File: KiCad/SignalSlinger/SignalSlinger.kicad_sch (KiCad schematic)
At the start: 65 parts, among them J101 Conn_01x02, J103 Conn_01x02, J104 Conn_01x02, J105 Conn_01x02, J106 Conn_01x02, J107 DB9 Female, J108 Conn_01x02, J109 Conn_01x03, J110 Conn_01x02, J111 Conn_01x03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

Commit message: Updates
o Updated Gerbers
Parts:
- removed C116: 10uF, Capacitor_SMD:C_0805_2012Metric, symbol Device:C_Small
- removed J105: Conn_01x02, Connector_PinSocket_2.54mm:PinSocket_1x02_P2.54mm_Vertical, symbol Connector_Generic:Conn_01x02
- removed J112: External Power Source, Connector_PinHeader_2.54mm:PinHeader_1x02_P2.54mm_Vertical, symbol Connector_Generic:Conn_01x02
- removed J113: Controlled Power, Connector_PinHeader_2.54mm:PinHeader_1x02_P2.54mm_Vertical, symbol Connector_Generic:Conn_01x02
- removed JP101: V-ext disable, Jumper:SolderJumper-2_P1.3mm_Bridged_RoundedPad1.0x1.5mm, symbol Jumper:SolderJumper_2_Bridged
- removed U105: TPS22810DBVT, Package_TO_SOT_SMD:SOT-23-6, symbol Power_Management:TPS22810DBVT
- added D111, D112: ESD9B5.0ST5G_1, Diode_SMD:D_0603_1608Metric, symbol Diode:ESD9B5.0ST5G_1
- added J102: Conn_01x03, Connector_PinHeader_2.54mm:PinHeader_1x03_P2.54mm_Vertical, symbol Connector_Generic:Conn_01x03
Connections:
- net GND: now also D111.2 (A2), D112.2 (A2), J102.2 (Pin_2)
- net Power_Good: now also U101.7 (PD1); no longer U101.11 (PD5)
- net Frequency Up: now reaches U101.12 (PD6/DAC)
- net Frequency Up: now also J107.4, D111.1 (A1), J102.3 (Pin_3)
- net Frequency Down: now reaches U101.13 (PD7)
- net Frequency Down: now also J107.5, D112.1 (A1), J102.1 (Pin_1)
- no-connect marks 18 -> 13
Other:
- note removed: "OPTIONAL AUX CONTROL"
- moved on the sheet: C104, D101, D102, D103, D104, D105, D106, D108, D109, D110, J101, J103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

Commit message: KiCad Updates
Updated Gerbers and schematic
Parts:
- added J105: Conn_01x04, Connector_PinHeader_2.54mm:PinHeader_1x04_P2.54mm_Vertical, symbol Connector_Generic:Conn_01x04
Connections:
- net GND: now also J105.1 (Pin_1)
- net Paddle Dah: now also J105.3 (Pin_3)
- net Paddle_Dit: now also J105.2 (Pin_2)
- net Straightkey: now also J105.4 (Pin_4)
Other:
- note added: "L101: 9T (24 cm) #24 Bifilar FT-50A-43"
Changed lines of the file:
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@@
     (effects (font (size 1.27 1.27)) (justify left bottom))
   )
+  (text "L101:\n9T (24 cm) #24 Bifilar FT-50A-43" (at 256.54 68.58 0)
+    (effects (font (size 0.9906 0.9906) (thickness 0.1981) bold) (justify left bottom))
+  )
   (text "I2C pull-ups can be provided by uC \nport pin pull-ups on SCL and SDA."
     (at 154.94 88.9 0)
@@
     )
   )
+  (global_label "Straightkey" (shape input) (at 160.02 175.26 0) (fields_autoplaced)
+    (effects (font (size 1 1)) (justify left))
+    (property "Intersheet References" "${INTERSHEET_REFS}" (id 0) (at 170.2533 175.1975 0)
+      (effects (font (size 1 1)) (justify left) hide)
+    )
+  )
   (global_label "CLK1" (shape output) (at 175.26 60.96 0) (fields_autoplaced)
     (effects (font (size 0.9906 0.9906)) (justify left))
@@
     )
   )
+  (global_label "Paddle_Dit" (shape input) (at 160.02 170.18 0) (fields_autoplaced)
+    (effects (font (size 1 1)) (justify left))
+    (property "Intersheet References" "${INTERSHEET_REFS}" (id 0) (at 169.8248 170.1175 0)
+      (effects (font (size 1 1)) (justify left) hide)
+    )
+  )
   (global_label "FET_DRIVER_ENABLE" (shape output) (at 80.01 71.12 0) (fields_autoplaced)
     (effects (font (size 0.9906 0.9906)) (justify left))
@@
     )
   )
+  (global_label "Paddle Dah" (shape input) (at 160.02 172.72 0) (fields_autoplaced)
+    (effects (font (size 1 1)) (justify left))
+    (property "Intersheet References" "${INTERSHEET_REFS}" (id 0) (at 170.5867 172.6575 0)
+      (effects (font (size 1 1)) (justify left) hide)
+    )
+  )
   (global_label "Fan_Contr" (shape output) (at 44.45 111.76 180) (fields_autoplaced)
     (effects (font (size 0.9906 0.9906)) (justify right))
@@
     (pin "1")
   )
+  (symbol (lib_id "power:GND") (at 160.02 167.64 90) (unit 1)
+    (in_bom yes) (on_board yes) (fields_autoplaced)
+    (property "Reference" "#PWR0166" (id 0) (at 166.37 167.64 0)
+      (effects (font (size 1.27 1.27)) hide)
+    )
+    (property "Value" "GND" (id 1) (at 164.4634 167.64 0)
+      (effects (font (size 1.27 1.27)) hide)
+    )
+    (property "Footprint" "" (id 2) (at 160.02 167.64 0)
+      (effects (font (size 1.27 1.27)) hide)
+    )
+    (property "Datasheet" "" (id 3) (at 160.02 167.64 0)
+      (effects (font (size 1.27 1.27)) hide)
+    )
+    (pin "1")
+  )
   (symbol (lib_id "Diode:ESD9B5.0ST5G_1") (at 139.7 137.16 270) (unit 1)
     (in_bom yes) (on_board yes) (fields_autoplaced)
@@
     (pin "2")
   )
+  (symbol (lib_id "Connector_Generic:Conn_01x04") (at 154.94 170.18 0) (mirror y) (unit 1)
+    (in_bom yes) (on_board yes) (fields_autoplaced)
+    (property "Reference" "J105" (id 0) (at 154.94 165.2072 0))
+    (property "Value" "Conn_01x04" (id 1) (at 154.94 165.2071 0)
+      (effects (font (size 1.27 1.27)) hide)
+    )
+    (property "Footprint" "Connector_PinHeader_2.54mm:PinHeader_1x04_P2.54mm_Vertical" (id 2) (at 154.94 170.18 0)
+      (effects (font (size 1.27 1.27)) hide)
+    )
+    (property "Datasheet" "~" (id 3) (at 154.94 170.18 0)
+      (effects (font (size 1.27 1.27)) hide)
+    )
+    (pin "1")
+    (pin "2")
+    (pin "3")
+    (pin "4")
+  )
   (symbol (lib_id "Device:C_Small") (at 260.35 57.15 90) (unit 1)
     (in_bom yes) (on_board yes)
@@
       (reference "#PWR0164") (unit 1) (value "GND") (footprint "")
     )
+    (path "/b7c888bf-e50e-45b8-8886-9bc5abf637fe/f25afcc1-fcb9-4c17-a20d-0ea083f083ef"
+      (reference "#PWR0165") (unit 1) (value "+3V3") (footprint "")
+    )
+    (path "/550b26c9-1cee-47c6-81a9-45e6d70bb39c"
+      (reference "#PWR0166") (unit 1) (value "GND") (footprint "")
+    )
     (path "/b7c888bf-e50e-45b8-8886-9bc5abf637fe/80c237a1-ee53-4ac9-8ec4-43aca92dc707"
       (reference "#PWR0201") (unit 1) (value "GND") (footprint "")
@@
     )
     (path "/b7c888bf-e50e-45b8-8886-9bc5abf637fe/01d30a66-451a-43fd-95f2-0bdd2117103d"
-      (reference "C213") (unit 1) (value "22uF") (footprint "Capacitor_SMD:C_1210_3225Metric")
+      (reference "C213") (unit 1) (value "22uF") (footprint "Capacitor_SMD:C_0805_2012Metric")
     )
     (path "/b7c888bf-e50e-45b8-8886-9bc5abf637fe/ebba386f-ca53-469e-b170-4c68f88638d5"
-      (reference "C214") (unit 1) (value "22uF") (footprint "Capacitor_SMD:C_1210_3225Metric")
+      (reference "C214") (unit 1) (value "22uF") (footprint "Capacitor_SMD:C_0805_2012Metric")
     )
     (path "/b7c888bf-e50e-45b8-8886-9bc5abf637fe/5c012b10-83b8-496d-af4b-de5dc92abc05"
-      (reference "C215") (unit 1) (value "22uF") (footprint "Capacitor_SMD:C_1210_3225Metric")
+      (reference "C215") (unit 1) (value "22uF") (footprint "Capacitor_SMD:C_0805_2012Metric")
     )
     (path "/b7c888bf-e50e-45b8-8886-9bc5abf637fe/1e940795-b9b5-45f3-99c7-d1d40e53f1a6"
@@
       (reference "C301") (unit 1) (value "470nF") (footprint "Capacitor_SMD:C_0805_2012Metric")
     )
-    (path "/da189f43-fd1f-445a-980b-345fda8b9a74/1e903e0b-fffc-4a7b-9e11-b17f2dc58886"
+    (path "/da189f43-fd1f-445a-980b-345fda8b9a74/f0d89eae-86d0-4eee-82c6-ad3daf7543e5"
       (reference "C302") (unit 1) (value "1100pF") (footprint "Capacitor_THT:C_Rect_L7.0mm_W2.5mm_P5.00mm")
     )
@@
       (reference "J104") (unit 1) (value "Conn_01x02") (footprint "Connector_PinSocket_2.54mm:PinSocket_1x02_P2.54mm_Vertical")
     )
+    (path "/db76a492-e672-4dba-bea7-c36487286d56"
+      (reference "J105") (unit 1) (value "Conn_01x04") (footprint "Connector_PinHeader_2.54mm:PinHeader_1x04_P2.54mm_Vertical")
+    )
     (path "/aad2424a-3937-4bc7-96c8-78c666e64a3d"
       (reference "J106") (unit 1) (value "Conn_01x02") (footprint "Connector_PinSocket_2.54mm:PinSocket_1x02_P2.54mm_Vertical")
@@
     )
     (path "/b7c888bf-e50e-45b8-8886-9bc5abf637fe/b1a6cee7-c293-4248-bf6c-e4b6e388a068"
-      (reference "L201") (unit 1) (value "2.2uH") (footprint "Inductor_SMD:L_Wuerth_WE-LQS")
+      (reference "L201") (unit 1) (value "2.2uH") (footprint "Inductor_SMD:WPN4020H2R2MT")
     )
     (path "/b7c888bf-e50e-45b8-8886-9bc5abf637fe/0c5297a9-41d0-4223-b152-7bff564be51e"
@@
       (reference "R204") (unit 1) (value "1M") (footprint "Resistor_SMD:R_0805_2012Metric")
     )
-    (path "/b7c888bf-e50e-45b8-8886-9bc5abf637fe/a604157e-b596-422f-8a01-c3245280c807"
+    (path "/b7c888bf-e50e-45b8-8886-9bc5abf637fe/846f2c13-278f-48b2-82e1-5d1c7211b810"
       (reference "R205") (unit 1) (value "105k") (footprint "Resistor_SMD:R_0805_2012Metric")
     )

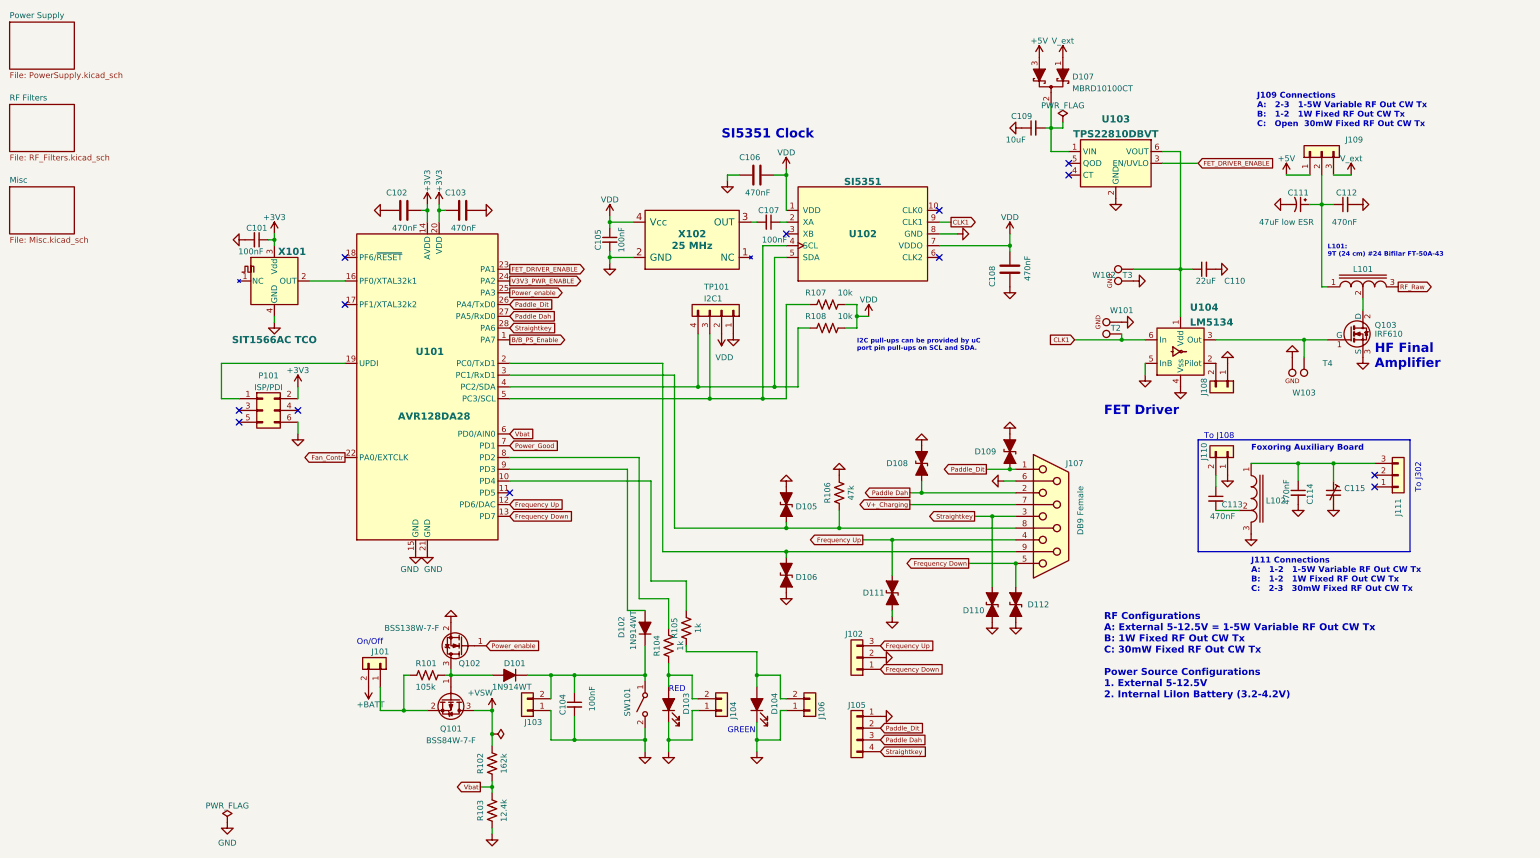
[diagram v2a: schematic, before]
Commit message: Schematic Updates
o Added support for a linear adjustable voltage regulator
o Added a switch
o Re-arranged components for a better fit
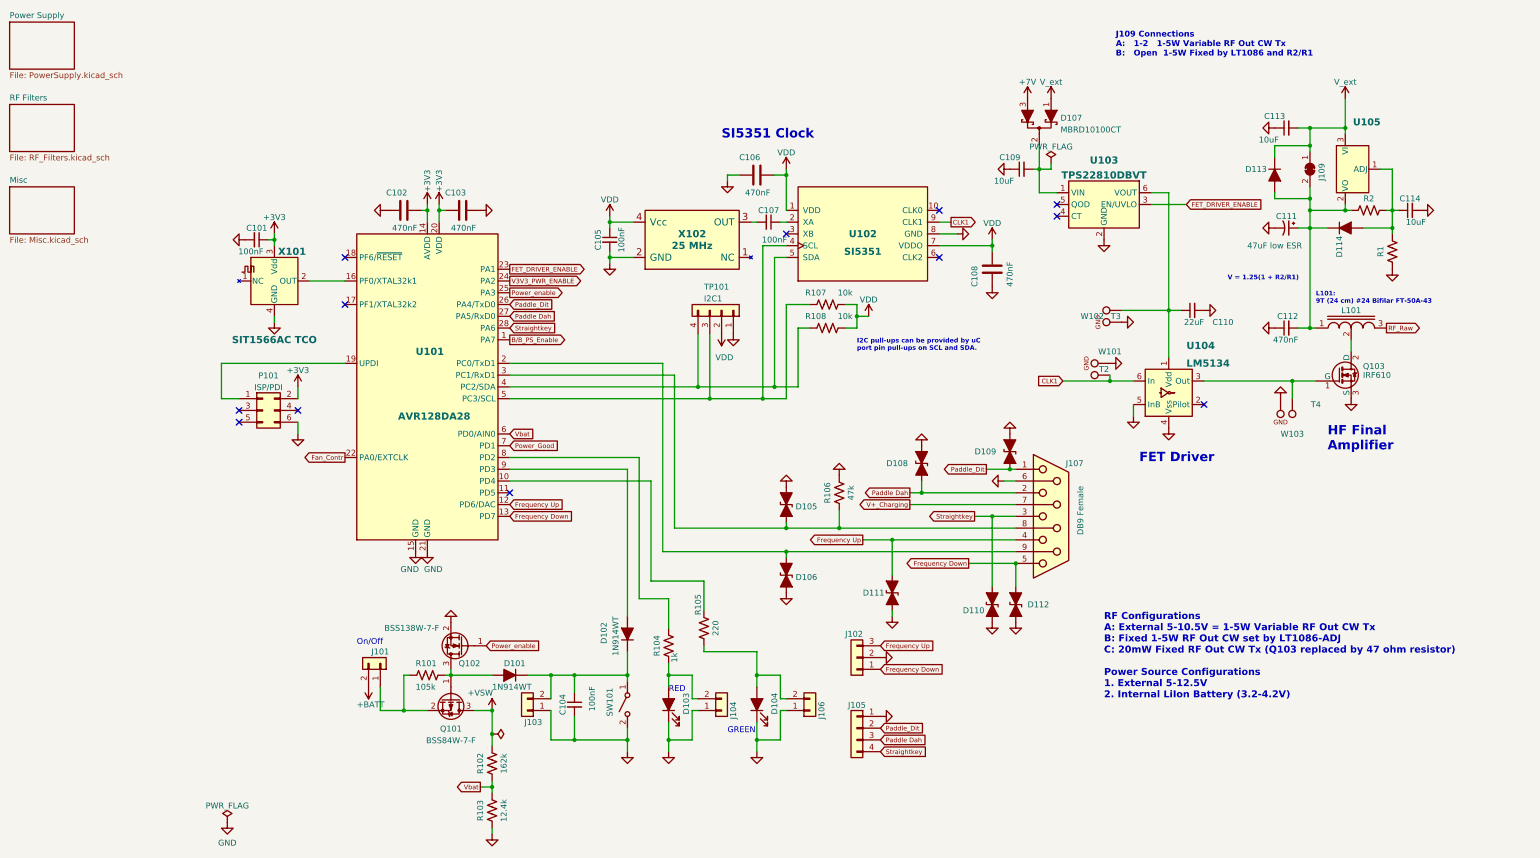
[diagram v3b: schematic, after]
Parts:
- removed C115: C_Trim_Small, Capacitors:MURATA-TZC3, symbol Device:C_Trim_Small
- removed J108, J110: Conn_01x02, Connector_PinHeader_2.54mm:PinHeader_1x02_P2.54mm_Vertical, symbol Connector_Generic:Conn_01x02
- removed J109, J111: Conn_01x03, Connector_PinHeader_2.54mm:PinHeader_1x03_P2.54mm_Vertical, symbol Connector_Generic:Conn_01x03
- removed L102: INDUCTOR_tapped, Inductors:Toroid_T-50A_TH_BF_CT_Vertical, symbol Device:INDUCTOR_tapped
- added D113, D114: 1N914WT, Diode_SMD:D_SOD-523, symbol Diode:1N914WT
- added J109: SolderJumper_2_Bridged, Jumper:SolderJumper-2_P1.3mm_Bridged_RoundedPad1.0x1.5mm, symbol Jumper:SolderJumper_2_Bridged
- added R1, R2: TBD, Resistor_THT:R_Axial_DIN0204_L3.6mm_D1.6mm_P2.54mm_Vertical, symbol Device:R_Small_US
- added U105: (no value), TO_SOT_Packages:TO-220_Neutral123_Horizontal, symbol Regulator_Linear:LT1086-ADJ
- C113, C114: value 470nF -> 10uF; Digi-Key Part No. 478-9924-1-ND -> 445-14418-1-ND; LCSC Part Number C342818 -> C3843628; Link https://www.digikey.com/products/en?keywords=478-9924-1-ND -> https://www.digikey.com/short/p8qdn4mp; Manufacturer AVX Corporation -> TDK Corporation; Manufacturer PN 08051C474K4Z2A -> C2012X5R1V106K125AC
- R105: value 1k -> 220; Digi-Key Part No. RMCF0805FT1K00CT-ND -> 13-RC0805FR-10220RLCT-ND; LCSC Part Number C17513 -> (none); Link https://www.digikey.com/en/products/detail/stackpole-electr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 -> https://www.digikey.com/en/products/detail/yageo/rc0805fr-1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; Manufacturer Stackpole Electronics Inc -> Yageo; Manufacturer PN RMCF0805FT1K00 -> RC0805FR-10220RL
- SW101: footprint Button_Switch_SMD:SW_SPST_B3U-3000P-B -> Button_Switch_SMD:SW_SPST_TL3305A; Digi-Key Part No. SW1256CT-ND -> EG5042CT-ND; Link (none) -> https://www.digikey.com/en/products/detail/e-switch/TL1014B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; Manufacturer Omron Electronics Inc-EMC Div -> E-Switch; Manufacturer PN B3U-3000P-B -> TL1014BF160QG
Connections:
- net GND: now also C112.1, C113.1, R1.1; no longer C112.2
- net V_ext: now also C113.2, D113.1 (K), J109.1 (A), U105.3 (VI)
- net at C111.1, L101.1: now also C112.2, D113.2 (A), D114.1 (K), J109.2 (B), R2.2, U105.2 (VO); no longer C112.1
- net at C114.1: now also D114.2 (A), R1.2, R2.1, U105.1 (ADJ)
- net +5V renamed +7V
- no-connect marks 13 -> 12
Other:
- note added: "J109 Connections A: 1-2 1-5W Variable RF Out CW Tx B: Open 1-5W Fixed by LT1086 and R2/R1"
- note added: "RF Configurations A: External 5-10.5V = 1-5W Variable RF Out CW Tx B: Fixed 1-5W RF Out CW set by LT1086-ADJ C: 20mW Fixed RF Out CW Tx (Q103 replaced by 47 ohm resistor) Power Source Configurations 1. External 5-12.5V 2. Internal LiIon Battery (3.2-4.2V)"
- note added: "V = 1.25(1 + R2/R1)"
- note removed: "Foxoring Auxiliary Board"
- note removed: "J109 Connections A: 2-3 1-5W Variable RF Out CW Tx B: 1-2 1W Fixed RF Out CW Tx C: Open 30mW Fixed RF Out CW Tx"
- note removed: "J111 Connections A: 1-2 1-5W Variable RF Out CW Tx B: 1-2 1W Fixed RF Out CW Tx C: 2-3 30mW Fixed RF Out CW Tx"
- note removed: "RF Configurations A: External 5-12.5V = 1-5W Variable RF Out CW Tx B: 1W Fixed RF Out CW Tx C: 30mW Fixed RF Out CW Tx Power Source Configurations 1. External 5-12.5V 2. Internal LiIon Battery (3.2-4.2V)"
- note removed: "To J108"
- note removed: "To J302"
- moved on the sheet: C108, C109, C110, C111, D102, D107, L101, Q103, R105, SW101, U103, U104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

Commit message: Updated Schematic Rev
Rev 1.2
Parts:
- U105: value (none) -> TO-220 ADJ Reg.
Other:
- title: SignalSlinger Design -> SignalSlinger
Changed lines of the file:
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@@
   (paper "A4")
   (title_block
-    (title "SignalSlinger Design")
-    (date "2023-07-10")
-    (rev "1.1")
+    (title "SignalSlinger")
+    (date "2023-11-17")
+    (rev "1.2")
   )
   (junction (at 154.94 81.28) (diameter 0) (color 0 0 0 0)
@@
       (effects (font (size 1.5 1.5) bold) (justify left))
     )
-    (property "Value" "" (id 1) (at 281.94 41.91 90)
+    (property "Value" "TO-220 ADJ Reg." (id 1) (at 281.94 41.91 90)
       (effects (font (size 1.5 1.5) bold) (justify left))
     )
